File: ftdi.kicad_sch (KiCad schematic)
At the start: 36 parts

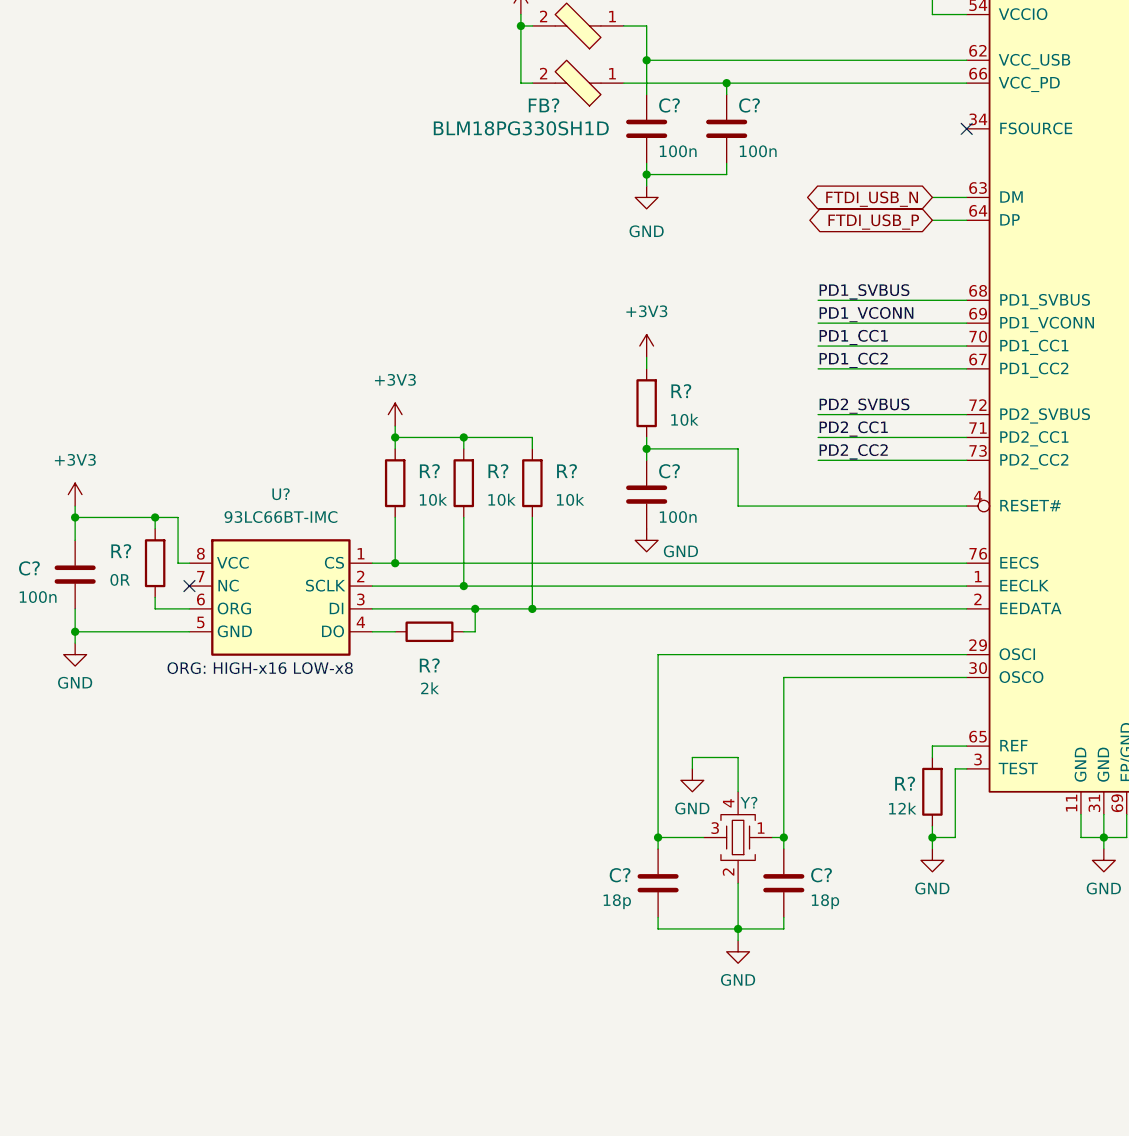
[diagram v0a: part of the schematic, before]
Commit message: Add missing PD interface connections
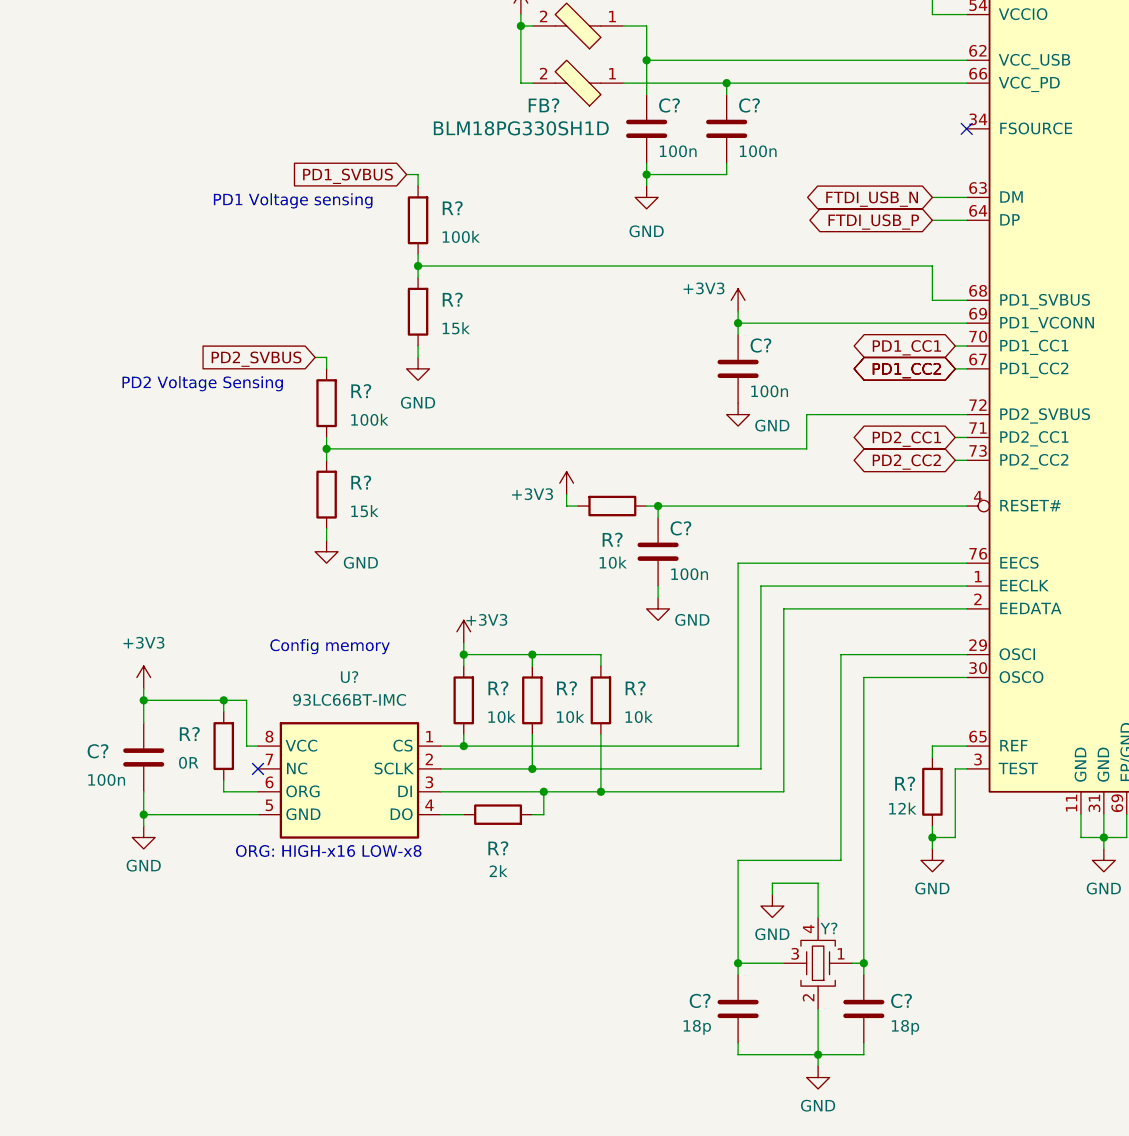
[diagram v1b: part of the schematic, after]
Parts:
- added C?: C_100n_0402, antmicro-footprints:0402-cap, symbol antmicroCapacitors0402:C_100n_0402
- added R? (x2): R_100k_0402, antmicro-footprints:0402-res, symbol antmicroResistors0402:R_100k_0402
- added R? (x2): R_15k_0402, antmicro-footprints:0402-res, symbol antmicroResistors0402:R_15k_0402
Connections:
- net PD1_VCONN is gone; now on net GND: U?.69 (PD1_VCONN)
- net +3V3: now also U?.69 (PD1_VCONN), C?.1
- net GND: now also C?.2, R?.1, R?.1
- net PD1_SVBUS: now also R?.2; no longer U?.68 (PD1_SVBUS)
- net PD2_SVBUS: now also R?.2; no longer U?.72 (PD2_SVBUS)
- new net: R?.1, R?.2, U?.72 (PD2_SVBUS)
- new net: R?.1, R?.2, U?.68 (PD1_SVBUS)
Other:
- note added: "Config memory"
- note added: "PD1 Voltage sensing"
- note added: "PD2 Voltage Sensing"
- moved on the sheet: C?, R?, U?, Y?
